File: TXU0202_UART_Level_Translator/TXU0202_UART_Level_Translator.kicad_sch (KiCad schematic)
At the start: 5 parts, among them J7 3V_SIDE, J7 5V_SIDE, U1 TXU0202DCUR

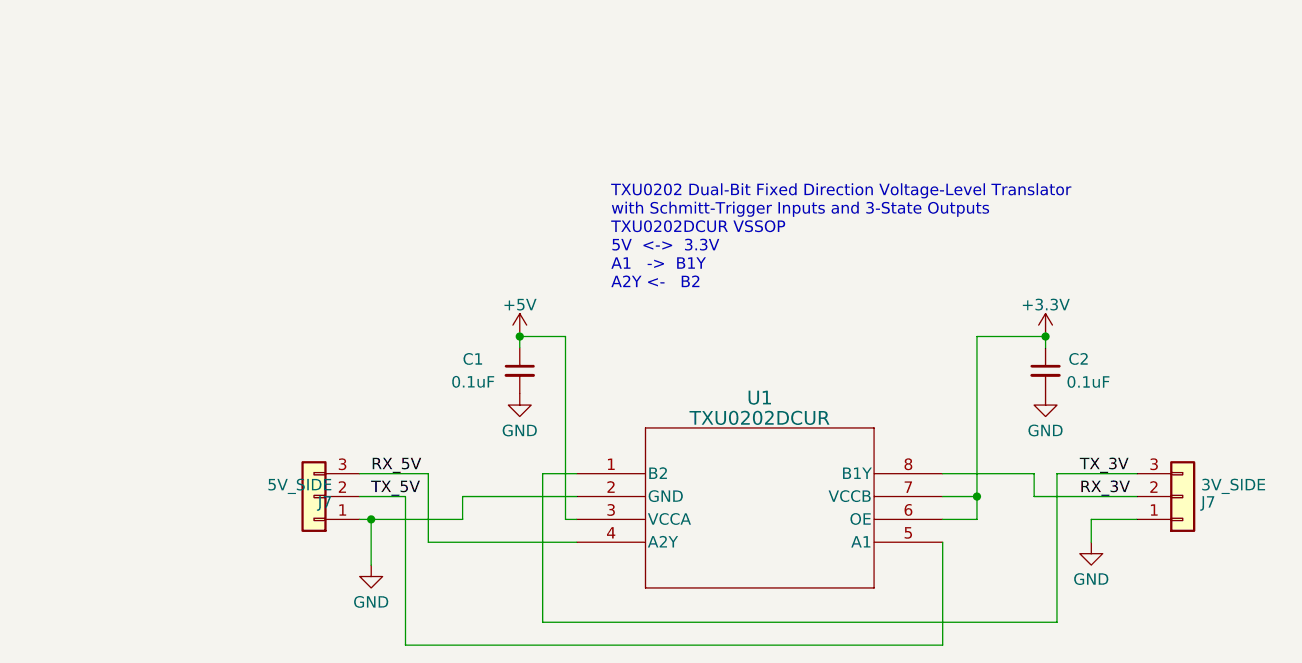
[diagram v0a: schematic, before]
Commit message: adding a few mew projects, most recent is Sallen_Key_Stage v1.0
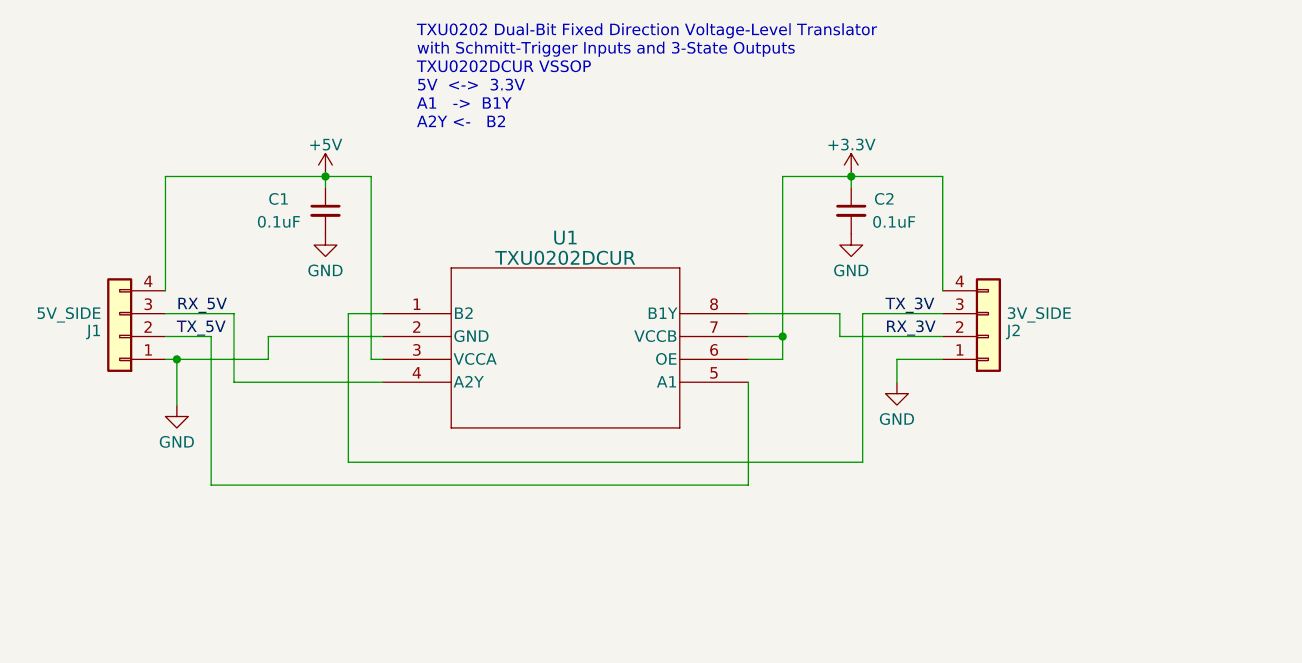
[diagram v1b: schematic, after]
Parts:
- removed J7: 3V_SIDE, Connector_PinHeader_2.54mm:PinHeader_1x03_P2.54mm_Horizontal, symbol Connector_Generic:Conn_01x03
- removed J7: 5V_SIDE, Connector_PinHeader_2.54mm:PinHeader_1x03_P2.54mm_Horizontal, symbol Connector_Generic:Conn_01x03
- added J1: 5V_SIDE, Connector_PinHeader_2.54mm:PinHeader_1x04_P2.54mm_Horizontal, symbol Connector_Generic:Conn_01x04
- added J2: 3V_SIDE, Connector_PinHeader_2.54mm:PinHeader_1x04_P2.54mm_Horizontal, symbol Connector_Generic:Conn_01x04
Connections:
- net +3.3V: now also J2.4 (Pin_4)
- net +5V: now also J1.4 (Pin_4)
- net GND: now also J1.1 (Pin_1), J2.1 (Pin_1)
- net RX_3V: now also J2.2 (Pin_2)
- net RX_5V: now also J1.3 (Pin_3)
- net TX_3V: now also J2.3 (Pin_3)
- net TX_5V: now also J1.2 (Pin_2)
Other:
- title: (none) -> UART Level Translator
- moved on the sheet: C1, C2, U1
